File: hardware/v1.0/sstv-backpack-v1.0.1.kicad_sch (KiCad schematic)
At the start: 11 parts, among them J1 Conn_01x03_Pin, J2 Conn_01x02_Pin, Q1 2N3904, SW1 SW_Push, SW2 SLW-1276864-4A-D, U1 ESP32-CAM

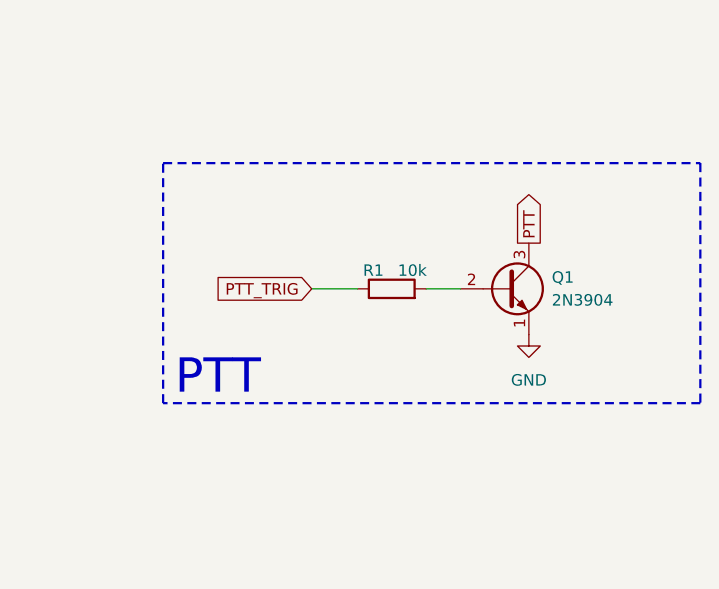
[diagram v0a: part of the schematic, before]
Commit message: Update README and add pull-down resistors for PTT
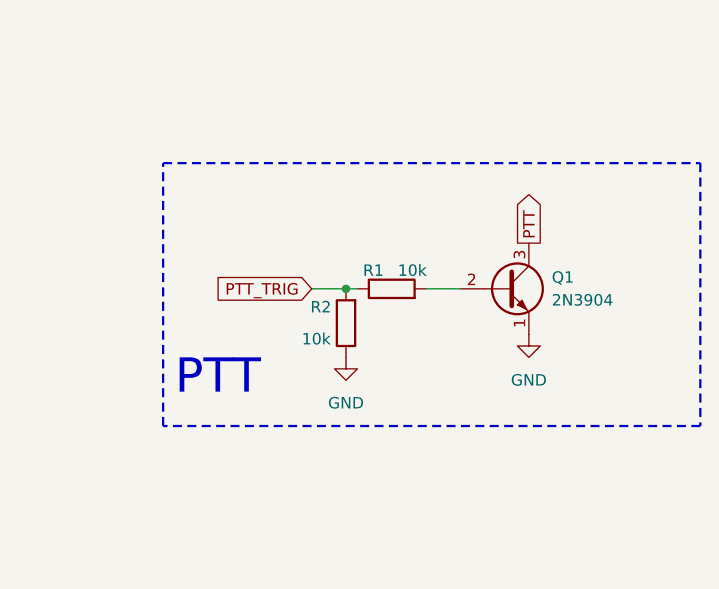
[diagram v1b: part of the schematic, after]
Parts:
- added R2: 10k, Resistor_THT:R_Axial_DIN0207_L6.3mm_D2.5mm_P7.62mm_Horizontal, symbol Device:R
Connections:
- net GND: now also R2.1
- net PTT_TRIG: now also R2.2
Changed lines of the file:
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@@
 	(rectangle
 		(start 190.5 93.98)
-		(end 250.19 120.65)
+		(end 250.19 123.19)
 		(stroke
 			(width 0.25)
@@
 		(color 0 0 0 0)
 	)
+	(junction
+		(at 210.82 107.95)
+		(diameter 0)
+		(color 0 0 0 0)
+	)
 	(no_connect
 		(at 66.04 129.54)
@@
 	(wire
 		(pts
-			(xy 207.01 107.95) (xy 212.09 107.95)
+			(xy 207.01 107.95) (xy 210.82 107.95)
 		)
 		(stroke
@@
 		(pts
 			(xy 110.49 81.28) (xy 110.49 82.55)
+		)
+		(stroke
+			(width 0)
+			(type default)
+		)
+	)
+	(wire
+		(pts
+			(xy 210.82 107.95) (xy 212.09 107.95)
 		)
 		(stroke
@@
 	)
 	(symbol
+		(lib_id "power:GND")
+		(at 210.82 115.57 0)
+		(unit 1)
+		(exclude_from_sim no)
+		(in_bom yes)
+		(on_board yes)
+		(dnp no)
+		(fields_autoplaced yes)
+		(property "Reference" "#PWR08"
+			(at 210.82 121.92 0)
+			(effects
+				(font
+					(size 1.27 1.27)
+				)
+				(hide yes)
+			)
+		)
+		(property "Value" "GND"
+			(at 210.82 120.65 0)
+			(effects
+				(font
+					(size 1.27 1.27)
+				)
+			)
+		)
+		(property "Footprint" ""
+			(at 210.82 115.57 0)
+			(effects
+				(font
+					(size 1.27 1.27)
+				)
+				(hide yes)
+			)
+		)
+		(property "Datasheet" ""
+			(at 210.82 115.57 0)
+			(effects
+				(font
+					(size 1.27 1.27)
+				)
+				(hide yes)
+			)
+		)
+		(property "Description" "Power symbol creates a global label with name \"GND\" , ground"
+			(at 210.82 115.57 0)
+			(effects
+				(font
+					(size 1.27 1.27)
+				)
+				(hide yes)
+			)
+		)
+		(pin "1"
+		)
+		(instances
+			(project "sstv-backpack-v1.0.1"
+				(path "/29ea68c4-1664-4e2a-8c4b-cdbccd245911"
+					(reference "#PWR08")
+					(unit 1)
+				)
+			)
+		)
+	)
+	(symbol
 		(lib_id "power:+5V")
 		(at 101.6 147.32 270)
@@
 					(unit 1)
 				)
+			)
+		)
+	)
+	(symbol
+		(lib_id "Device:R")
+		(at 210.82 111.76 180)
+		(unit 1)
+		(exclude_from_sim no)
+		(in_bom yes)
+		(on_board yes)
+		(dnp no)
+		(property "Reference" "R2"
+			(at 208.026 109.982 0)
+			(effects
+				(font
+					(size 1.27 1.27)
+				)
+			)
+		)
+		(property "Value" "10k"
+			(at 207.518 113.538 0)
+			(effects
+				(font
+					(size 1.27 1.27)
+				)
+			)
+		)
+		(property "Footprint" "Resistor_THT:R_Axial_DIN0207_L6.3mm_D2.5mm_P7.62mm_Horizontal"
+			(at 212.598 111.76 90)
+			(effects
+				(font
+					(size 1.27 1.27)
+				)
+				(hide yes)
+			)
+		)
+		(property "Datasheet" "~"
+			(at 210.82 111.76 0)
+			(effects
+				(font
+					(size 1.27 1.27)
+				)
+				(hide yes)
+			)
+		)
+		(property "Description" "Resistor"
+			(at 210.82 111.76 0)
+			(effects
+				(font
+					(size 1.27 1.27)
+				)
+				(hide yes)
+			)
+		)
+		(pin "1"
+		)
+		(pin "2"
+		)
+		(instances
+			(project "sstv-backpack-v1.0.1"
+				(path "/29ea68c4-1664-4e2a-8c4b-cdbccd245911"
+					(reference "R2")
+					(unit 1)
+				)
